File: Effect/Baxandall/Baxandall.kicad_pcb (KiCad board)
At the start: 2 copper layers, 32 x 75 mm, 24 parts, among them J1 Conn_01x04_Pin, J2 Conn_01x03_Pin, U1 OPA1656

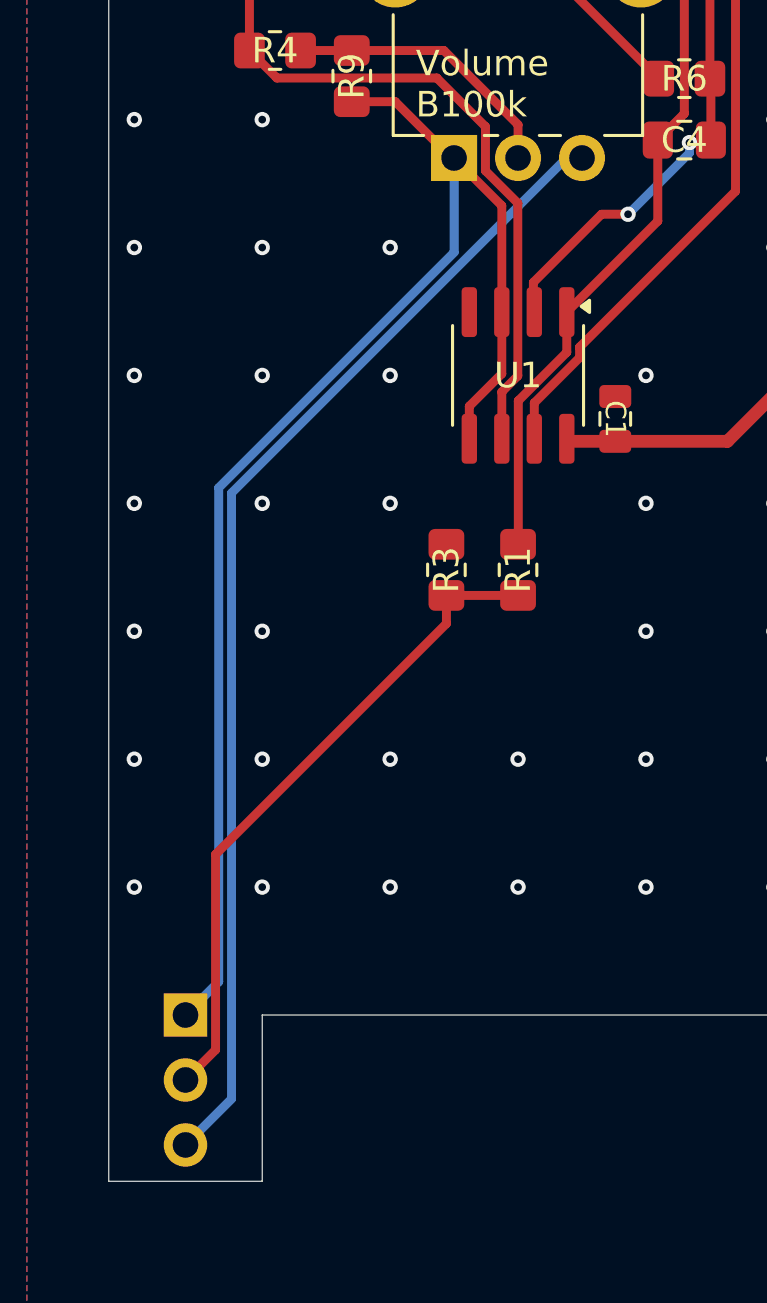
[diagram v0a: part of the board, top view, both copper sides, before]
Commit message: Baxandall: remove unnecessary output resistors
These came from the TI reference design, and I kept them around until I
actually put the board together, at which point I went "I like the
tinkering, but not pointlessly".

So remove them.

I'm not sure why that 47kΩ resistor to ground was there.  As some kind
of preemptive DC biasing for the next stage with a capacitive input? Not
relevant for this design.

Signed-off-by: Linus Torvalds <torvalds@linux-foundation.org>
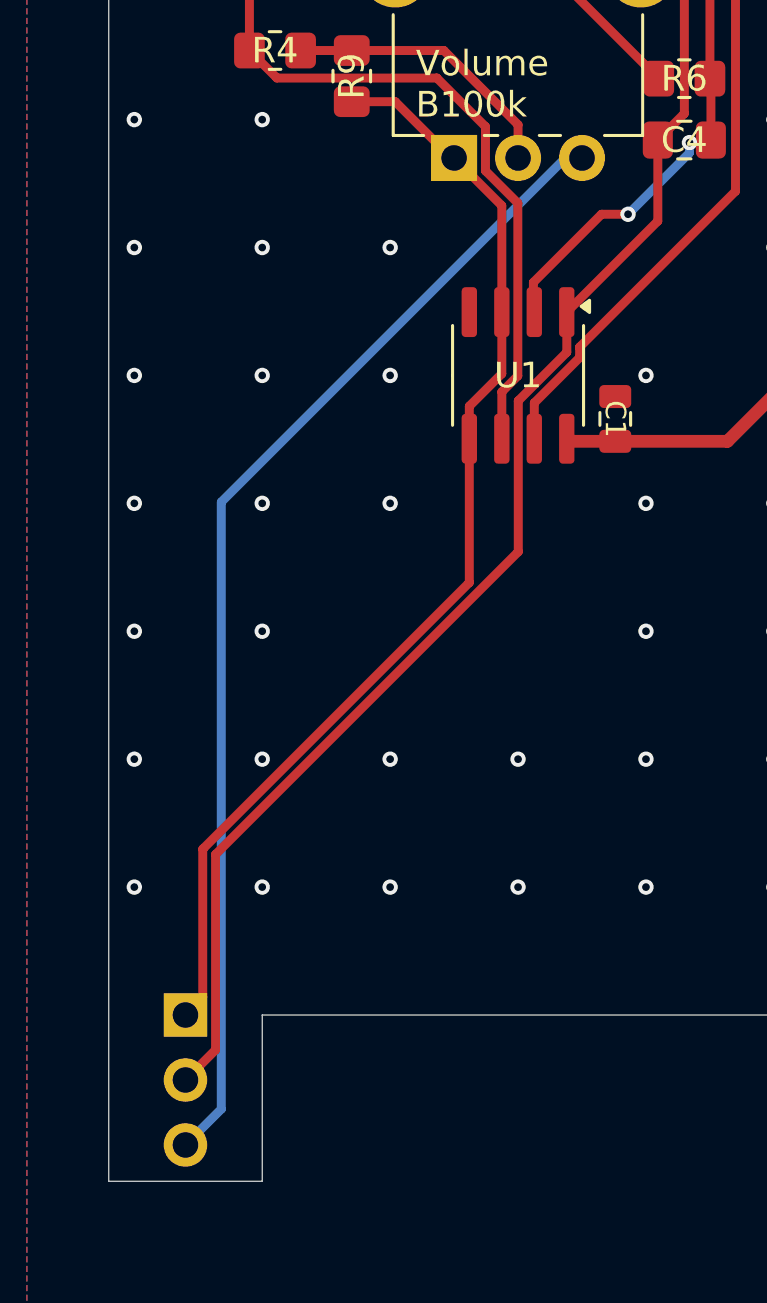
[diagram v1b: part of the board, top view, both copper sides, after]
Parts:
- removed R1: 100R, Resistor_SMD:R_0805_2012Metric_Pad1.20x1.40mm_HandSolder
- removed R3: 47k, Resistor_SMD:R_0805_2012Metric_Pad1.20x1.40mm_HandSolder
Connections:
- J2 pad 2: OUT -> OPAMP^{OUT}
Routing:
- net OPAMP^{OUT}: track 40.9 -> 67.0 mm
- net OUT: track 26.0 -> 0.00 mm
- net GNDREF: track 55.0 -> 44.3 mm
